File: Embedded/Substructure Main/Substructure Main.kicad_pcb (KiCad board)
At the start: 4 copper layers, 40 x 30 mm, 60 parts, among them J2 MicroSD, U10 INA220AIDGSR, U11 Sensored, U6 LD1117S33TR_SOT223, U7 LD1117S50TR_SOT223, U8 USB2513B_Bi, U9 MCP7940N-xMNY, Y1 TSX-3225 24MF18X-C0, Y2 CM7V-T1A

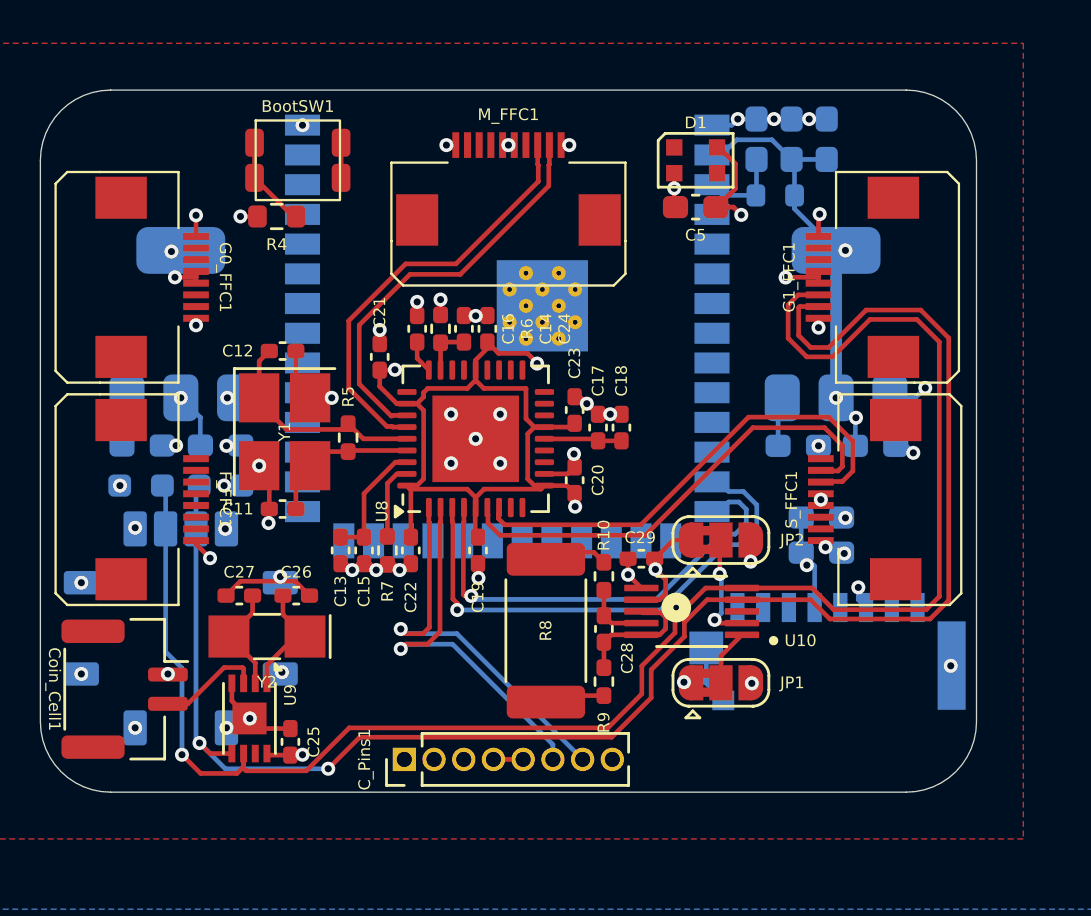
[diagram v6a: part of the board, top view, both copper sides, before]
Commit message: Removed Power Sensor
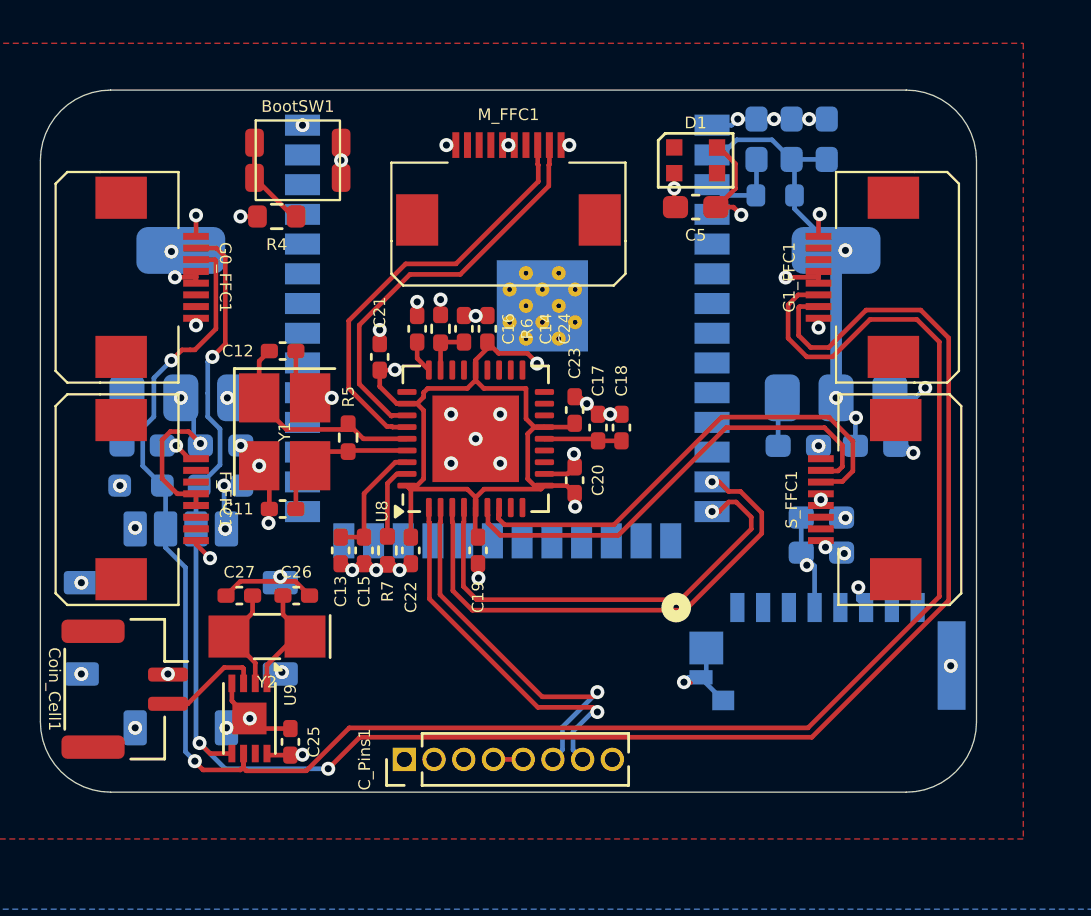
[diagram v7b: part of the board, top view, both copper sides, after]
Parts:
- removed C28: 1uF, Capacitor_SMD:C_0402_1005Metric_Pad0.74x0.62mm_HandSolder
- removed C29: 0.1uF, Capacitor_SMD:C_0402_1005Metric_Pad0.74x0.62mm_HandSolder
- removed JP1, JP2: Bit Set, Jumper:SolderJumper-3_P1.3mm_Bridged2Bar12_RoundedPad1.0x1.5mm
- removed R10, R9: 10, Resistor_SMD:R_0402_1005Metric_Pad0.72x0.64mm_HandSolder
- removed R8: Shunt CRF2512-FZ-R002ELF, Resistor_SMD:R_2512_6332Metric_Pad1.40x3.35mm_HandSolder
- removed U10: INA220AIDGSR, INA220:SOP50P490X110-10N
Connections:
- M_FFC1 pad 5: +5VP -> +5VS
- M_FFC1 pad 6: +5VP -> +5VS
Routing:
- net I2C SCL: track 72.4 -> 82.8 mm, vias 1 -> 2
- net I2C SDA: track 70.9 -> 81.3 mm, vias 2 -> 3
- net +5V: track 12.7 -> 18.6 mm, vias 6 -> 7
- net Net-(U10-VBUS): track 5.59 -> 0.00 mm
- net Net-(JP2-C): track 4.81 -> 0.00 mm, vias 2 -> 0
- net GND: track 59.0 -> 54.8 mm
- net +5VP: track 4.56 -> 1.40 mm, vias 1 -> 0
- net Net-(U10-VIN-): track 2.82 -> 0.00 mm
- net Net-(JP1-C): track 2.42 -> 0.00 mm
- net +5VS: track 6.74 -> 4.75 mm, vias 0 -> 1
- net HUD USB -: track 16.6 -> 15.8 mm
- net +3V3: track 67.2 -> 66.6 mm, vias 19 -> 16
- added copper zone on B.Cu, net +3V3
- added copper zone on In1.Cu, net +5V
- added copper zone on In2.Cu, net GND
- removed copper zone on In2.Cu, net +3V3
- removed copper zone on B.Cu, net GND
- removed copper zone on In1.Cu, net GND

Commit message: Modified Fills
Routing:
- net +5VS: track 4.75 -> 51.9 mm, vias 1 -> 4
- net Net-(ESP1-GPIO0/BOOT): track 3.96 -> 18.0 mm, vias 0 -> 1
- net +3V3: track 66.6 -> 67.9 mm
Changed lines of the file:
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@@
 	)
 	(segment
+		(start 113.35 65.5)
+		(end 113.35 65.750001)
+		(width 0.2)
+		(layer "F.Cu")
+		(net 2)
+	)
+	(segment
 		(start 88.5435 70.989)
 		(end 90.25 70.989)
@@
 	)
 	(segment
-		(start 92.85 53)
-		(end 92.85 53.75)
-		(width 0.2)
-		(layer "F.Cu")
-		(net 2)
-	)
-	(segment
 		(start 86.65 69.4)
 		(end 87.25 70)
@@
 	)
 	(segment
+		(start 92.85 52.25)
+		(end 92.85 53.75)
+		(width 0.2)
+		(layer "F.Cu")
+		(net 2)
+	)
+	(segment
 		(start 95.622502 70.2375)
 		(end 95.35 70.510002)
@@
 	)
 	(segment
-		(start 92.85 52.25)
-		(end 92.85 53)
-		(width 0.2)
-		(layer "F.Cu")
-		(net 2)
-	)
-	(segment
 		(start 85.45 74.975)
 		(end 85.45 74.95)
@@
 	)
 	(via
-		(at 92.85 53)
+		(at 92.85 52.25)
 		(size 0.6)
 		(drill 0.3)
@@
 	)
 	(via
-		(at 113.249376 65.2)
+		(at 113.35 65.5)
 		(size 0.6)
 		(drill 0.3)
@@
 	)
 	(segment
+		(start 87.7 66.75)
+		(end 86.649999 66.75)
+		(width 0.2)
+		(layer "F.Cu")
+		(net 3)
+	)
+	(segment
 		(start 101.5375 64.4)
 		(end 102.6675 64.4)
@@
 	)
 	(segment
+		(start 87.85 66.9)
+		(end 87.7 66.75)
+		(width 0.2)
+		(layer "F.Cu")
+		(net 3)
+	)
+	(segment
 		(start 98.241798 67.051)
 		(end 98.6 67.409202)
@@
 	)
 	(segment
+		(start 89.95 56.375)
+		(end 90.925 55.4)
+		(width 0.2)
+		(layer "F.Cu")
+		(net 37)
+	)
+	(segment
+		(start 89.95 56.5)
+		(end 89.95 56.375)
+		(width 0.2)
+		(layer "F.Cu")
+		(net 37)
+	)
+	(via
+		(at 89.95 56.5)
+		(size 0.6)
+		(drill 0.3)
+		(layers "F.Cu" "B.Cu")
+		(net 37)
+	)
+	(segment
+		(start 90.25 68.01)
+		(end 89.95 67.71)
+		(width 0.2)
+		(layer "B.Cu")
+		(net 37)
+	)
+	(segment
+		(start 89.95 67.71)
+		(end 89.95 56.5)
+		(width 0.2)
+		(layer "B.Cu")
+		(net 37)
+	)
+	(segment
+		(start 91.2 68.01)
+		(end 90.25 68.01)
+		(width 0.2)
+		(layer "B.Cu")
+		(net 37)
+	)
+	(segment
 		(start 111.95 59.1809)
 		(end 112.3809 58.75)
@@
 	)
 	(segment
-		(start 99.75 52.35)
-		(end 100 52.35)
+		(start 100 51.65)
+		(end 99.75 51.9)
 		(width 0.2)
 		(layer "F.Cu")
@@
 	)
 	(segment
-		(start 100 52.35)
+		(start 100.250001 52.749999)
 		(end 100.250001 52.35)
 		(width 0.2)
@@
 		(net 96)
 	)
+	(segment
+		(start 100 53)
+		(end 100.250001 52.749999)
+		(width 0.2)
+		(layer "F.Cu")
+		(net 96)
+	)
+	(segment
+		(start 99.75 51.9)
+		(end 99.75 52.35)
+		(width 0.2)
+		(layer "F.Cu")
+		(net 96)
+	)
+	(segment
+		(start 99.75 52.75)
+		(end 99.75 52.35)
+		(width 0.2)
+		(layer "F.Cu")
+		(net 96)
+	)
+	(segment
+		(start 100 53.1)
+		(end 100 53)
+		(width 0.2)
+		(layer "F.Cu")
+		(net 96)
+	)
+	(segment
+		(start 100.250001 51.900001)
+		(end 100.250001 52.35)
+		(width 0.2)
+		(layer "F.Cu")
+		(net 96)
+	)
+	(segment
+		(start 100 51.65)
+		(end 100.250001 51.900001)
+		(width 0.2)
+		(layer "F.Cu")
+		(net 96)
+	)
+	(segment
+		(start 100 53)
+		(end 99.75 52.75)
+		(width 0.2)
+		(layer "F.Cu")
+		(net 96)
+	)
 	(via
-		(at 100 52.35)
+		(at 111.7 63.15)
 		(size 0.6)
 		(drill 0.3)
@@
 		(net 96)
 	)
+	(via
+		(at 81.853057 63.144784)
+		(size 0.6)
+		(drill 0.3)
+		(layers "F.Cu" "B.Cu")
+		(net 96)
+	)
+	(via
+		(at 100 53.1)
+		(size 0.6)
+		(drill 0.3)
+		(layers "F.Cu" "B.Cu")
+		(net 96)
+	)
+	(via
+		(at 100 51.65)
+		(size 0.6)
+		(drill 0.3)
+		(layers "F.Cu" "B.Cu")
+		(net 96)
+	)
+	(segment
+		(start 83.7 63.15)
+		(end 81.858273 63.15)
+		(width 0.5)
+		(layer "B.Cu")
+		(net 96)
+	)
+	(segment
+		(start 81.858273 63.15)
+		(end 81.853057 63.144784)
+		(width 0.2)
+		(layer "B.Cu")
+		(net 96)
+	)
 	(segment
 		(start 111.524376 63.325624)
@@
 	)
 	(segment
+		(start 99.15 53.95)
+		(end 85.9 53.95)
+		(width 0.5)
+		(layer "In1.Cu")
+		(net 96)
+	)
+	(segment
+		(start 100 53.1)
+		(end 101.65 53.1)
+		(width 0.5)
+		(layer "In1.Cu")
+		(net 96)
+	)
+	(segment
+		(start 100 53.1)
+		(end 99.15 53.95)
+		(width 0.5)
+		(layer "In1.Cu")
+		(net 96)
+	)
+	(segment
+		(start 85.9 53.95)
+		(end 81.853057 57.996943)
+		(width 0.5)
+		(layer "In1.Cu")
+		(net 96)
+	)
+	(segment
+		(start 100 51.65)
+		(end 100 53.1)
+		(width 0.5)
+		(layer "In1.Cu")
+		(net 96)
+	)
+	(segment
+		(start 101.65 53.1)
+		(end 111.7 63.15)
+		(width 0.5)
+		(layer "In1.Cu")
+		(net 96)
+	)
+	(segment
+		(start 81.853057 57.996943)
+		(end 81.853057 63.144784)
+		(width 0.5)
+		(layer "In1.Cu")
+		(net 96)
+	)
+	(segment
 		(start 88.6825 74.723)
 		(end 88.6335 74.674)
@@
 		(min_thickness 0.25)
 		(filled_areas_thickness no)
-		(fill
+		(fill yes
 			(thermal_gap 0.5)
 			(thermal_bridge_width 0.5)
@@
 		(polygon
 			(pts
-				(xy 74.95 45) (xy 125 45) (xy 125 85) (xy 75 85)
+				(xy 75 45) (xy 125 45) (xy 125 85) (xy 75 85)
 			)
 		)
@@
 		(min_thickness 0.25)
 		(filled_areas_thickness no)
-		(fill
+		(fill yes
 			(thermal_gap 0.5)
 			(thermal_bridge_width 0.5)
@@
 		(min_thickness 0.25)
 		(filled_areas_thickness no)
-		(fill
+		(fill yes
 			(thermal_gap 0.5)
 			(thermal_bridge_width 0.5)
